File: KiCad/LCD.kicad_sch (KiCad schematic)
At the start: 4 parts

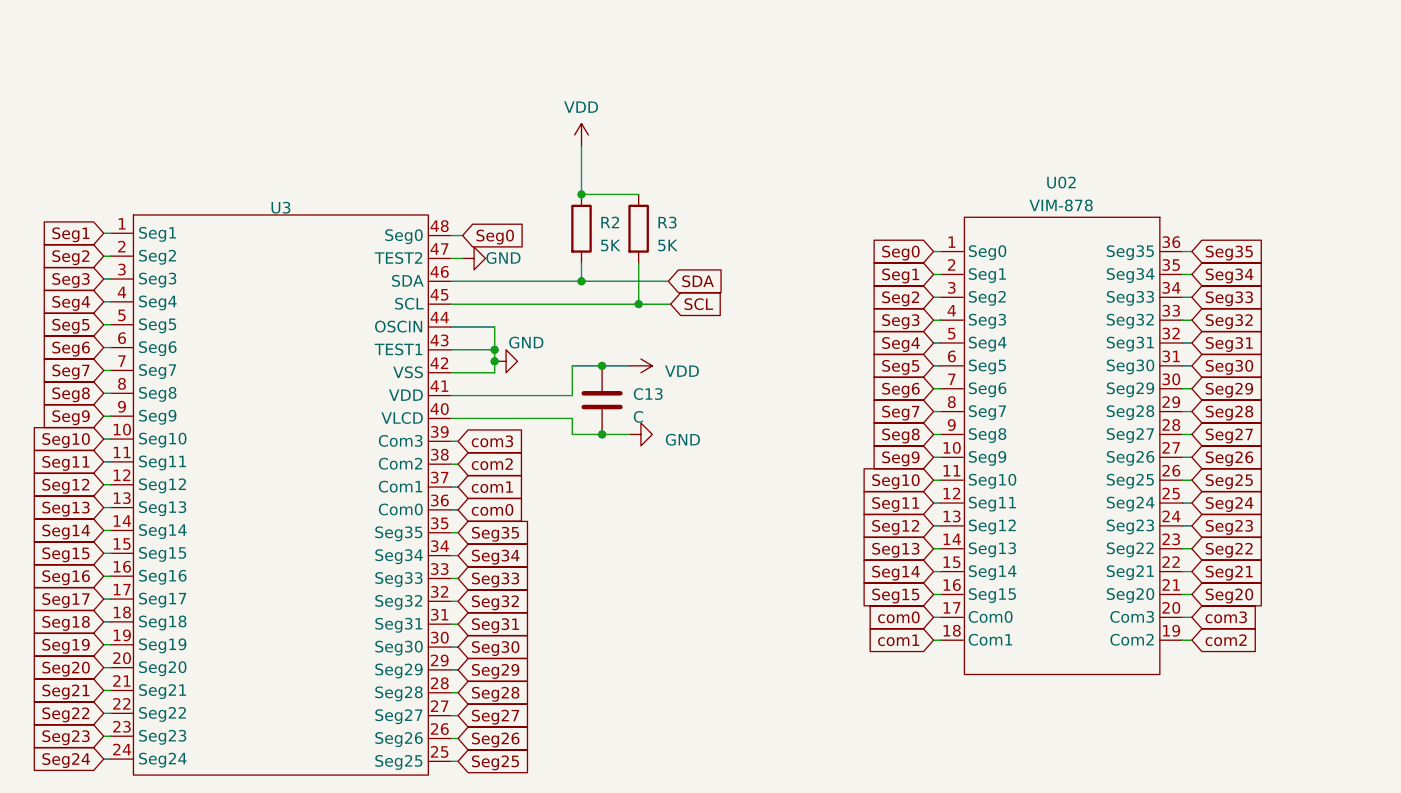
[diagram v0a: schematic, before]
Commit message: added power schematic to design
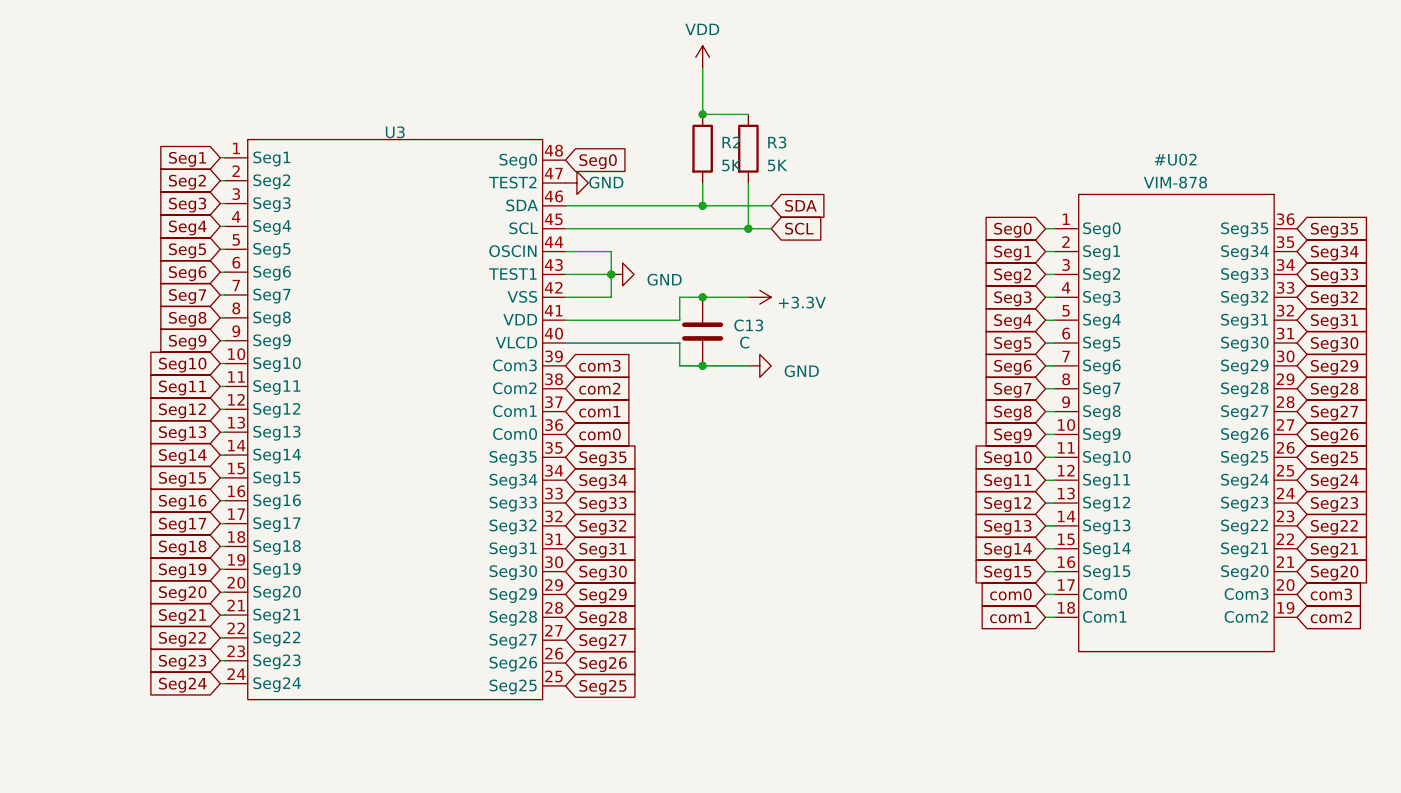
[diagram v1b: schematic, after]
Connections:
- net VDD: no longer C13.1, U3.41 (VDD)
- new net +3.3V: C13.1, U3.41 (VDD)
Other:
- moved on the sheet: C13, R2, R3, U3
